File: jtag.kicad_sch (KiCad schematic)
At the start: 4 parts, among them IC1 FT232HL-REEL

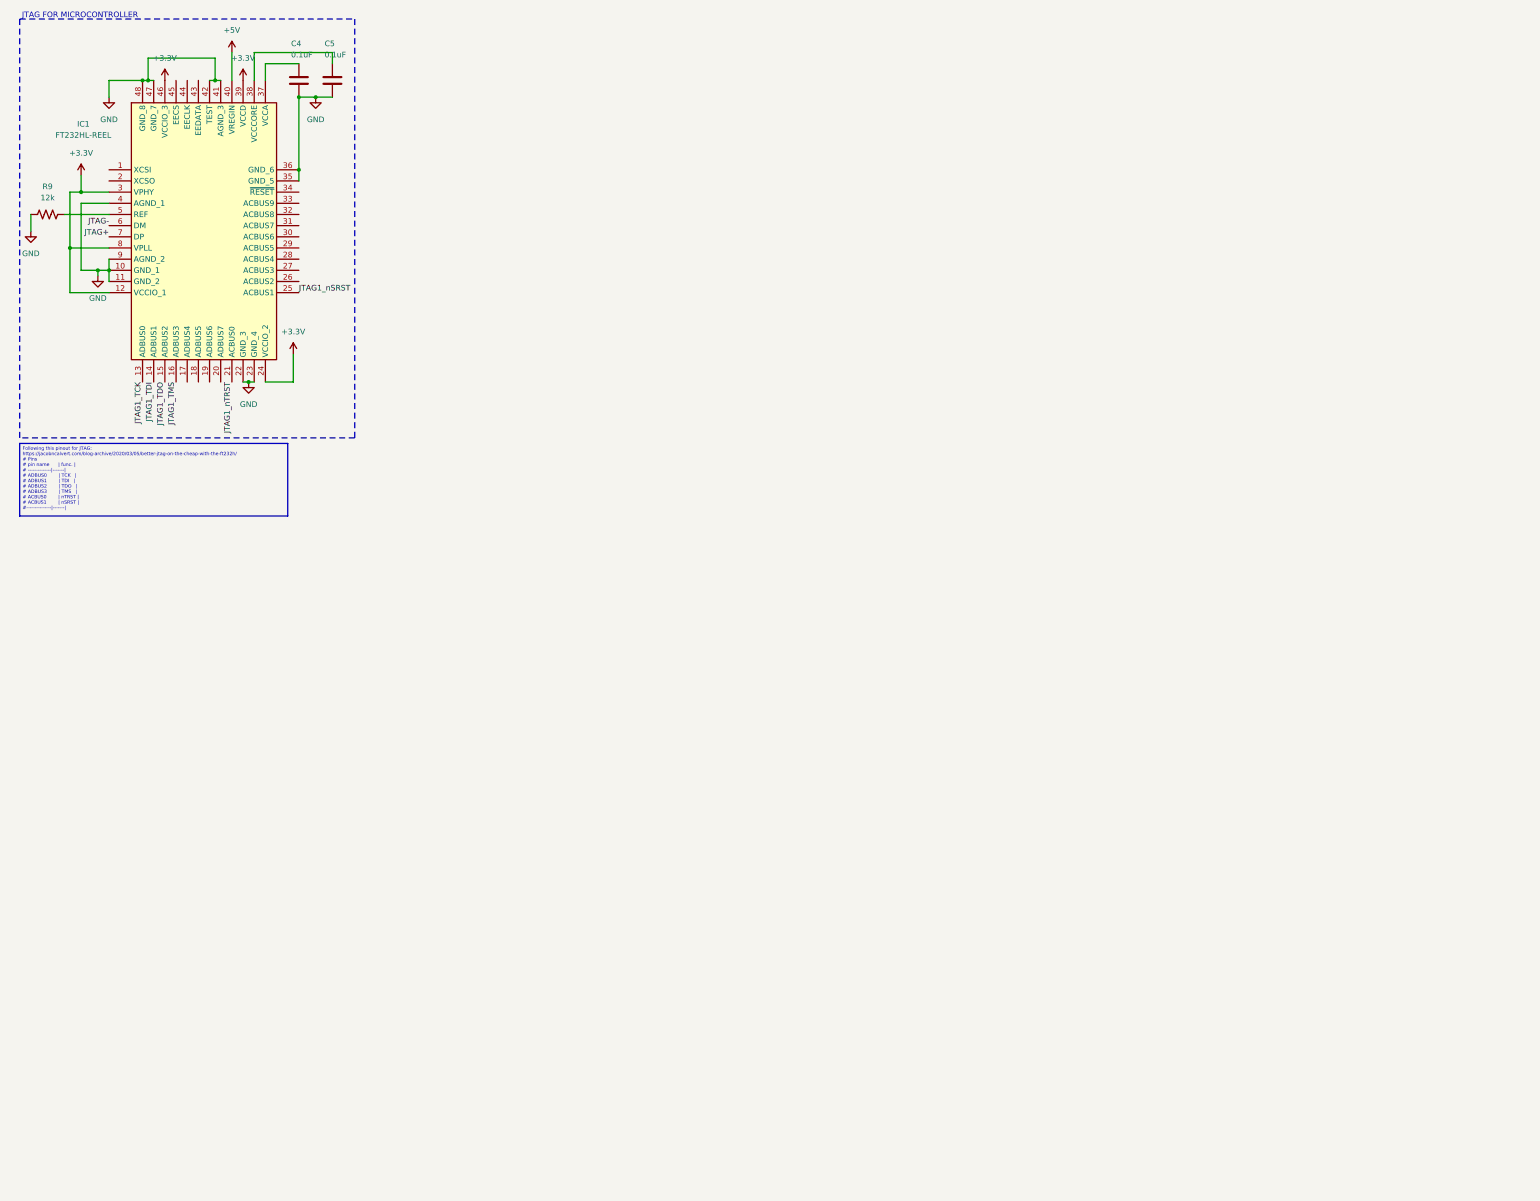
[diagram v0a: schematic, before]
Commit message: Used steppenprobe as base for our UART and JTAG.
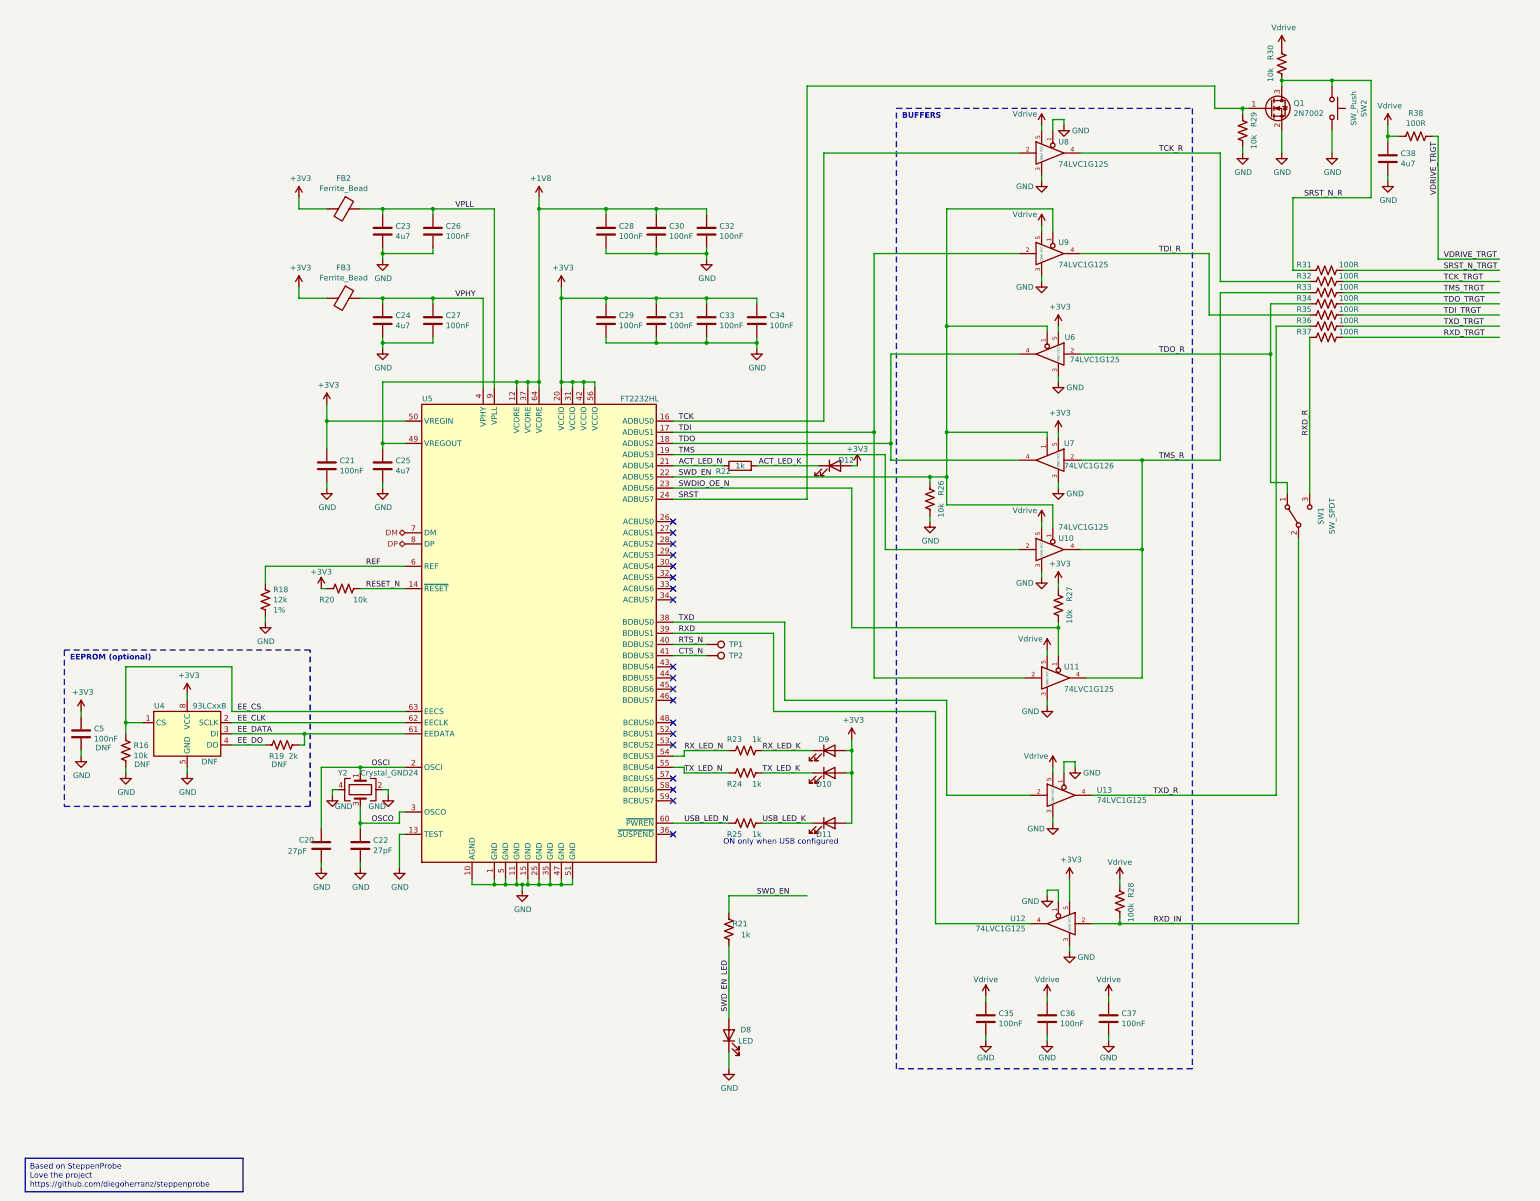
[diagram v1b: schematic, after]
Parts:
- removed C4: 0.1uF, symbol Device:C
- removed IC1: FT232HL-REEL, QFP50P900X900X160-48N, symbol SamacSys_Parts:FT232HL-REEL
- removed R9: 12k, symbol Device:R_US
- added C20, C22: 27pF, Capacitor_SMD:C_0603_1608Metric, symbol Device:C
- added C21, C26, C27, C28, C29, C30, C31, C32, C33, C34, C35, C36, C37: 100nF, Capacitor_SMD:C_0603_1608Metric, symbol Device:C
- added C23, C24, C25, C38: 4u7, Capacitor_SMD:C_0603_1608Metric, symbol Device:C
- added D10, D11, D12, D8, D9: LED, LED_SMD:LED_0603_1608Metric, symbol Device:LED
- added FB2, FB3: Ferrite_Bead, Inductor_SMD:L_0603_1608Metric, symbol Device:Ferrite_Bead
- added Q1: 2N7002, Package_TO_SOT_SMD:SOT-23, symbol Transistor_FET:2N7002
- added R16, R20, R26, R27, R29, R30: 10k, Resistor_SMD:R_0603_1608Metric, symbol Device:R_US
- added R18: 12k, Resistor_SMD:R_0603_1608Metric, symbol Device:R_US
- added R19: 2k, Resistor_SMD:R_0603_1608Metric, symbol Device:R_US
- added R21, R23, R24, R25: 1k, Resistor_SMD:R_0603_1608Metric, symbol Device:R_US
- added R22: 1k, Resistor_SMD:R_0603_1608Metric, symbol Device:R
- added R28: 100k, Resistor_SMD:R_0603_1608Metric, symbol Device:R_US
- added R31, R32, R33, R34, R35, R36, R37, R38: 100R, Resistor_SMD:R_0603_1608Metric, symbol Device:R_US
- added SW1: SW_SPDT, Button_Switch_SMD:SW_SPDT_PCM12, symbol Switch:SW_SPDT
- added SW2: SW_Push, Button_Switch_SMD:SW_Push_1P1T_NO_E-Switch_TL3301NxxxxxG, symbol Switch:SW_Push
- added TP1, TP2: TestPoint, TestPoint:TestPoint_Pad_D1.0mm, symbol Connector:TestPoint
- added U10, U11, U12, U13, U6, U8, U9: 74LVC1G125, Package_TO_SOT_SMD:SOT-353_SC-70-5, symbol 74xxGxx_power_pins:74LVC1G125-74xGxx
- added U4: 93LCxxB, Package_SO:SOIC-8_3.9x4.9mm_P1.27mm, symbol Memory_EEPROM:93LCxxB
- added U5: FT2232HL, Package_QFP:LQFP-64_10x10mm_P0.5mm, symbol Interface_USB:FT2232HL
- added U7: 74LVC1G126, Package_TO_SOT_SMD:SOT-353_SC-70-5, symbol 74xxGxx_power_pins:74LVC1G126-74xGxx
- added Y2: Crystal_GND24, Crystal:Crystal_SMD_3225-4Pin_3.2x2.5mm, symbol Device:Crystal_GND24
- C5: value 0.1uF -> 100nF; footprint (none) -> Capacitor_SMD:C_0603_1608Metric; kibom_fit (none) -> DNF
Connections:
- net GND: now also C20.2, C21.2, C22.2, C23.2, C24.2, C25.2, C26.2, C27.2, C28.2, C29.2, C30.2, C31.2, C32.2, C33.2, C34.2, C35.2, C36.2, C37.2, C38.2, D8.1 (K), Q1.2 (S), R16.2, R18.2, R26.1, R29.1, SW2.2, U10.3 (GND), U11.3 (GND), U12.1, U12.3 (GND), U13.1, U13.3 (GND), U4.5 (GND), U5.1 (GND), U5.10 (AGND), U5.11 (GND), U5.13 (TEST), U5.15 (GND), U5.25 (GND), U5.35 (GND), U5.47 (GND), U5.5 (GND), U5.51 (GND), U6.3 (GND), U7.3 (GND), U8.1, U8.3 (GND), U9.3 (GND), Y2.2, Y2.4
- net +3V3: now reaches C5.1
- net +3V3: now also C21.1, C29.1, C31.1, C33.1, C34.1, D10.2 (A), D11.2 (A), D12.2 (A), D9.2 (A), FB2.2, FB3.2, R20.2, R27.2, U12.5 (VCC), U4.8 (VCC), U5.20 (VCCIO), U5.31 (VCCIO), U5.42 (VCCIO), U5.50 (VREGIN), U5.56 (VCCIO), U6.5 (VCC), U7.5 (VCC)
- new net +1V8: C25.1, C28.1, C30.1, C32.1, U5.12 (VCORE), U5.37 (VCORE), U5.49 (VREGOUT), U5.64 (VCORE)
- new net ACT_LED_K: D12.1 (K), R22.2
- new net ACT_LED_N: R22.1, U5.21 (ADBUS4)
- new net CTS_N: TP2.1, U5.41 (BDBUS3)
- new net DM: U5.7 (DM)
- new net DP: U5.8 (DP)
- new net EE_CLK: U4.2 (SCLK), U5.62 (EECLK)
- new net EE_CS: R16.1, U4.1 (CS), U5.63 (EECS)
- new net EE_DATA: R19.2, U4.3 (DI), U5.61 (EEDATA)
- new net EE_DO: R19.1, U4.4 (DO)
- new net OSCI: C20.1, U5.2 (OSCI), Y2.1
- new net OSCO: C22.1, U5.3 (OSCO), Y2.3
- new net REF: R18.1, U5.6 (REF)
- new net RESET_N: R20.1, U5.14 (~{RESET})
- new net RTS_N: TP1.1, U5.40 (BDBUS2)
- new net RXD: U12.4, U5.39 (BDBUS1)
- new net RXD_IN: R28.1, SW1.2 (B), U12.2
- new net RXD_R: R37.1, SW1.3 (C)
- new net RXD_TRGT: R37.2
- new net RX_LED_K: D9.1 (K), R23.1
- new net RX_LED_N: R23.2, U5.54 (BCBUS3)
- new net SRST: Q1.1 (G), R29.2, U5.24 (ADBUS7)
- new net SRST_N_R: Q1.3 (D), R30.1, R31.2, SW2.1
- new net SRST_N_TRGT: R31.1
- new net SWDIO_OE_N: R27.1, U11.1, U5.23 (ADBUS6)
- new net SWD_EN: R21.2, R26.2, U10.1, U5.22 (ADBUS5), U6.1, U7.1, U9.1
- new net SWD_EN_LED: D8.2 (A), R21.1
- new net TCK: U5.16 (ADBUS0), U8.2
- new net TCK_R: R32.2, U8.4
- new net TCK_TRGT: R32.1
- new net TDI: U11.2, U5.17 (ADBUS1), U9.2
- new net TDI_R: R35.2, U9.4
- new net TDI_TRGT: R35.1
- new net TDO: U5.18 (ADBUS2), U6.4, U7.4
- new net TDO_R: R34.2, SW1.1 (A), U6.2
- new net TDO_TRGT: R34.1
- new net TMS: U10.2, U5.19 (ADBUS3)
- new net TMS_R: R33.2, U10.4, U11.4, U7.2
- new net TMS_TRGT: R33.1
- new net TXD: U13.2, U5.38 (BDBUS0)
- new net TXD_R: R36.2, U13.4
- new net TXD_TRGT: R36.1
- new net TX_LED_K: D10.1 (K), R24.1
- new net TX_LED_N: R24.2, U5.55 (BCBUS4)
- new net USB_LED_K: D11.1 (K), R25.1
- new net USB_LED_N: R25.2, U5.60 (~{PWREN})
- new net VDRIVE_TRGT: R38.1
- new net VPHY: C24.1, C27.1, FB3.1, U5.4 (VPHY)
- new net VPLL: C23.1, C26.1, FB2.1, U5.9 (VPLL)
- new net Vdrive: C35.1, C36.1, C37.1, C38.1, R28.2, R30.2, R38.2, U10.5 (VCC), U11.5 (VCC), U13.5 (VCC), U8.5 (VCC), U9.5 (VCC)
- no-connect marks 0 -> 19
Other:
- note added: "BUFFERS"
- note added: "EEPROM (optional)"
- note added: "ON only when USB configured"
- note removed: "JTAG FOR MICROCONTROLLER"

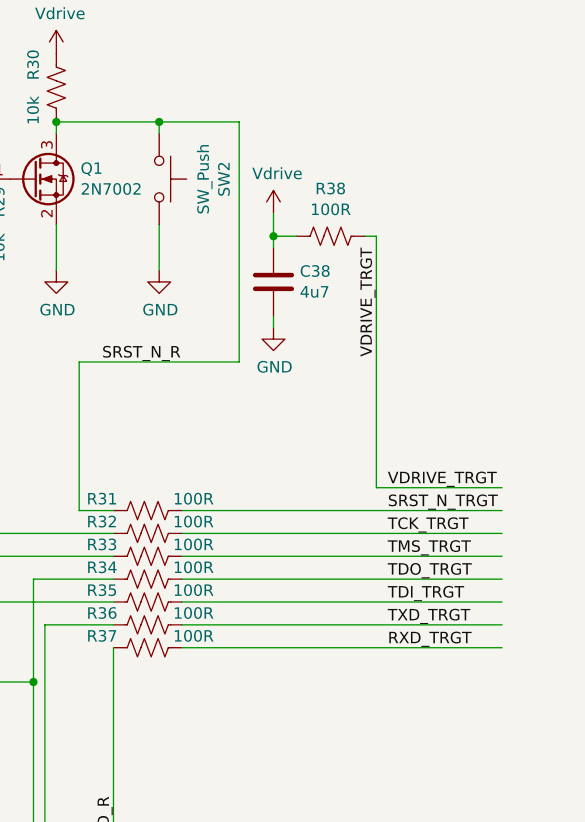
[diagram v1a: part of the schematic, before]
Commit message: updated edge connector
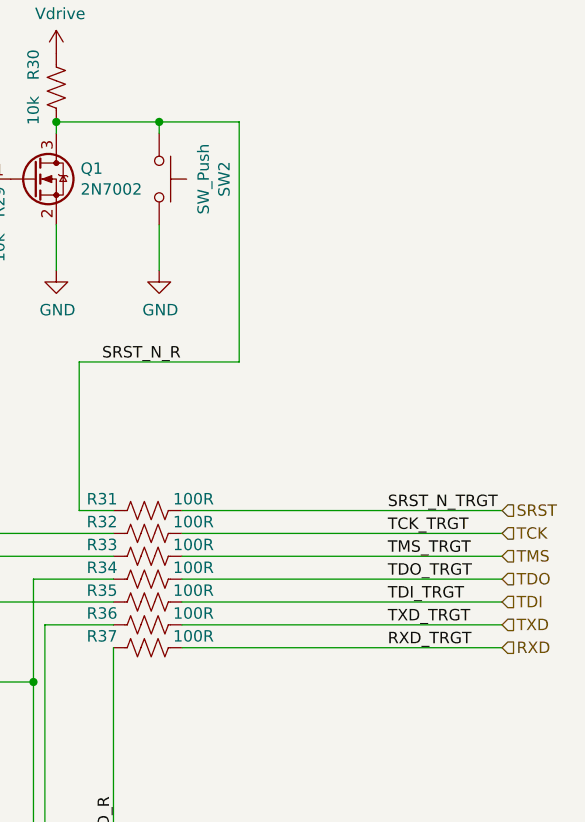
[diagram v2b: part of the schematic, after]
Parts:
- removed C38: 4u7, Capacitor_SMD:C_0603_1608Metric, symbol Device:C
- removed R38: 100R, Resistor_SMD:R_0603_1608Metric, symbol Device:R_US
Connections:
- net RXD_TRGT is gone; now on net RXD: R37.2
- net SRST_N_TRGT is gone; now on net SRST: R31.1
- net TCK_TRGT is gone; now on net TCK: R32.1
- net TDI_TRGT is gone; now on net TDI: R35.1
- net TDO_TRGT is gone; now on net TDO: R34.1
- net TMS_TRGT is gone; now on net TMS: R33.1
- net TXD_TRGT is gone; now on net TXD: R36.1

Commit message: started pcb layout, host and usbhub done
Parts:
- SW2: footprint Button_Switch_SMD:SW_Push_1P1T_NO_E-Switch_TL3301NxxxxxG -> Button_Switch_SMD:SW_Push_1P1T_XKB_TS-1187A
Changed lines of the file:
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@@
 			)
 		)
-		(property "Footprint" "Button_Switch_SMD:SW_Push_1P1T_NO_E-Switch_TL3301NxxxxxG"
+		(property "Footprint" "Button_Switch_SMD:SW_Push_1P1T_XKB_TS-1187A"
 			(at 317.5 36.83 0)
 			(effects

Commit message: pcb routed!!!!!!!
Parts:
- removed C35, C36, C37: 100nF, Capacitor_SMD:C_0603_1608Metric, symbol Device:C
- removed FB2, FB3: Ferrite_Bead, Inductor_SMD:L_0603_1608Metric, symbol Device:Ferrite_Bead
- removed Q1: 2N7002, Package_TO_SOT_SMD:SOT-23, symbol Transistor_FET:2N7002
- removed R26, R27, R29, R30: 10k, Resistor_SMD:R_0603_1608Metric, symbol Device:R_US
- removed R28: 100k, Resistor_SMD:R_0603_1608Metric, symbol Device:R_US
- removed SW1: SW_SPDT, Button_Switch_SMD:SW_SPDT_PCM12, symbol Switch:SW_SPDT
- removed SW2: SW_Push, Button_Switch_SMD:SW_Push_1P1T_XKB_TS-1187A, symbol Switch:SW_Push
- removed U10, U11, U12, U13, U6, U8, U9: 74LVC1G125, Package_TO_SOT_SMD:SOT-353_SC-70-5, symbol 74xxGxx_power_pins:74LVC1G125-74xGxx
- removed U7: 74LVC1G126, Package_TO_SOT_SMD:SOT-353_SC-70-5, symbol 74xxGxx_power_pins:74LVC1G126-74xGxx
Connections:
- net RXD_R is gone; now on net RXD: R37.1
- net SRST_N_R is gone; now on net SRST: R31.2
- net TCK_R is gone; now on net TCK: R32.2
- net TDI_R is gone; now on net TDI: R35.2
- net TDO_R is gone; now on net TDO: R34.2
- net TMS_R is gone; now on net TMS: R33.2
- net TXD_R is gone; now on net TXD: R36.2
- net VPHY is gone; now on net +3.3V: C24.1, C27.1, U5.4 (VPHY)
- net VPLL is gone; now on net +3.3V: C23.1, C26.1, U5.9 (VPLL)
- net RXD: no longer R37.2
- net SRST: no longer R31.1
- net TCK: no longer R32.1
- net TDI: no longer R35.1
- net TDO: no longer R34.1
- net TMS: no longer R33.1
- net TXD: no longer R36.1
- net +3V3 renamed +3.3V
- new net RXD_TRGT: R37.2
- new net SRST_TRGT: R31.1
- new net TCK_TRGT: R32.1
- new net TDI_TRGT: R35.1
- new net TDO_TRGT: R34.1
- new net TMS_TRGT: R33.1
- new net TXD_TRGT: R36.1
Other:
- note removed: "BUFFERS"
- moved on the sheet: R31, R32, R33, R34, R35, R36, R37
